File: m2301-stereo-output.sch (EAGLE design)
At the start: 77 parts, among them U1 ERM1-5MM, U2 ERM1-5MM, U3 ERM1-5MM, U4 G3VM-62C1

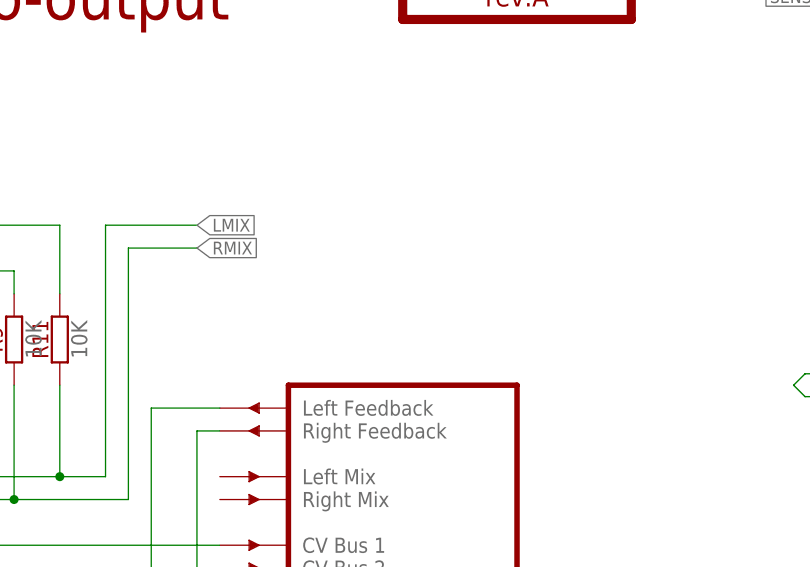
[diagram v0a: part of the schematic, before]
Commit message: Add (dummy) FX2 connectors to sch
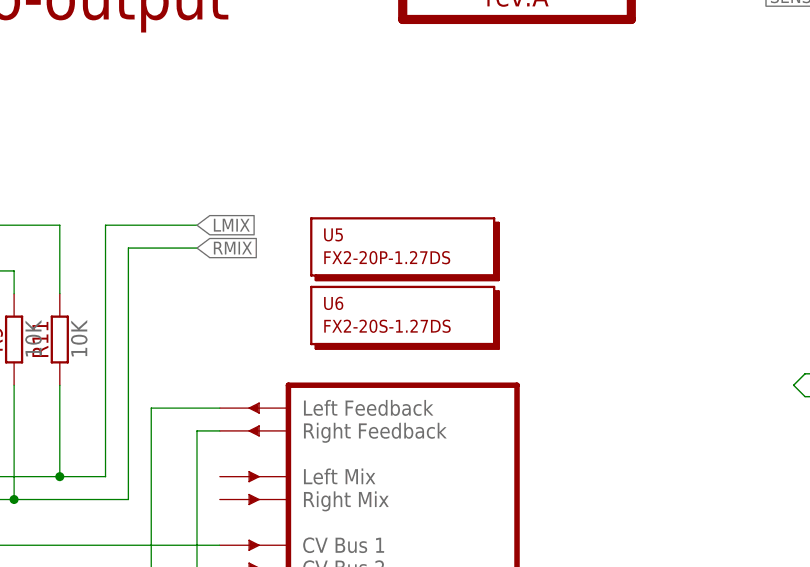
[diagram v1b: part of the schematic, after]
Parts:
- added U5: FX2-20P-1.27DS, hardware:FX2-20P-1.27DS
- added U6: FX2-20S-1.27DS, hardware:FX2-20S-1.27DS
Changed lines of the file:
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@@
 <part name="PWR6" library="supply" deviceset="-15V" device=""/>
 <part name="PWR7" library="supply" deviceset="-15V" device=""/>
+<part name="U5" library="hardware" deviceset="?" device="FX2-20P-1.27DS"/>
+<part name="U6" library="hardware" deviceset="?" device="FX2-20S-1.27DS"/>
 </parts>
 <sheets>
@@
 <instance part="PWR6" gate="G$1" x="160.02" y="-68.58" rot="R270"/>
 <instance part="PWR7" gate="G$1" x="160.02" y="-116.84" rot="R270"/>
+<instance part="U5" gate="G$1" x="109.22" y="12.7"/>
+<instance part="U6" gate="G$1" x="109.22" y="5.08"/>
 </instances>
 <busses>

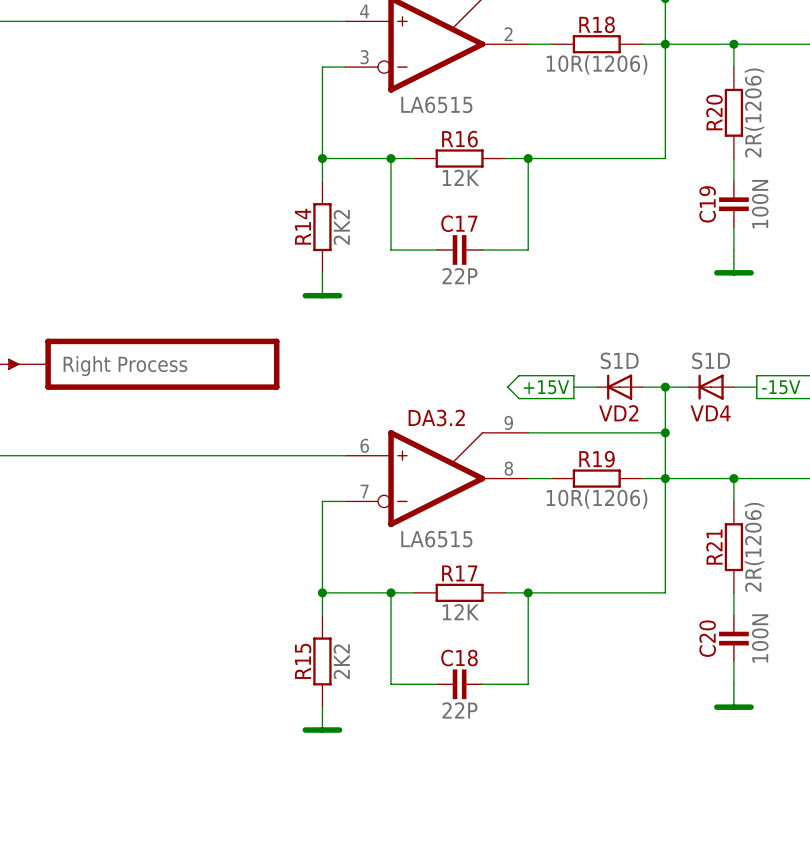
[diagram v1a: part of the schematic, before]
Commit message: Change headphone amplifier gain to +15 dB #4
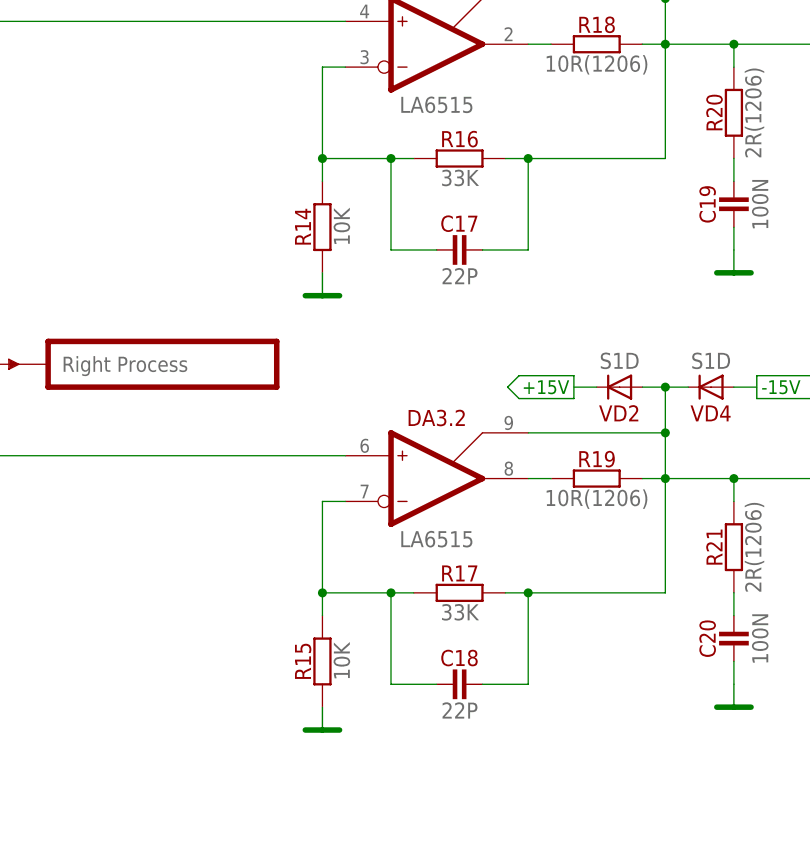
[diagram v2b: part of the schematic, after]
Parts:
- R14, R15: value 2K2 -> 10K; device resistors:2K2 -> resistors:10K
- R16, R17: value 12K -> 33K; device resistors:12K -> resistors:33K
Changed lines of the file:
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@@
 <?xml version="1.0" encoding="utf-8"?>
 <!DOCTYPE eagle SYSTEM "eagle.dtd">
-<eagle version="7.4.2">
+<eagle version="7.5.0">
 <drawing>
 <settings>
@@
 <part name="R19" library="resistors" deviceset="?" device="10R(1206)"/>
 <part name="DA3" library="ic-sanyo" deviceset="LA6515" device=""/>
-<part name="R14" library="resistors" deviceset="?" device="2K2"/>
-<part name="R15" library="resistors" deviceset="?" device="2K2"/>
-<part name="R16" library="resistors" deviceset="?" device="12K"/>
-<part name="R17" library="resistors" deviceset="?" device="12K"/>
+<part name="R14" library="resistors" deviceset="?" device="10K" value="10K"/>
+<part name="R15" library="resistors" deviceset="?" device="10K" value="10K"/>
+<part name="R16" library="resistors" deviceset="?" device="33K" value="33K"/>
+<part name="R17" library="resistors" deviceset="?" device="33K" value="33K"/>
 <part name="GND11" library="supply" deviceset="GND" device=""/>
 <part name="GND13" library="supply" deviceset="GND" device=""/>

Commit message: m2301 PCB update
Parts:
- removed HL1, HL2: WHITE(2MMX5MM), optoelectronics:WHITE(2MMX5MM)
- removed R24, R25: 100K, resistors:100K
- removed R27, R28: 680R, resistors:680R
- removed R3, R4: 10R(1206), resistors:10R(1206)
- removed U2, U3: ERM1-5MM, hardware:ERM1-5MM
- removed VD3, VD4: S1D, diodes:S1D
- removed VD6, VD7: MMSD4148, diodes:MMSD4148
- removed VT1, VT2: BC848, transistors-npn:BC848
- added C24, C25, C26, C27, C28: 100N, capacitors:100N
- added DA5: LM2903M, ic-fairchild:LM2903M
- added HL4: RED/BLUE(2MMX5MM,CC), optoelectronics:RED/BLUE(2MMX5MM,CC)
- added L1, L2: BLM31AJ601SN1L, inductors:BLM31AJ601SN1L
- added R30, R31: 10M, resistors:10M
- added R32, R33: 100K, resistors:100K
- added R34, R35: 47K, resistors:47K
- added R36: 330K, resistors:330K
- added R37: 22K, resistors:22K
- added R38: 4K7, resistors:4K7
- added R39: 100R, resistors:100R
- added R40: 2K2, resistors:2K2
- added R41: 10K, resistors:10K
- added R42: 1K8, resistors:1K8
- added U7: ERM1-5MM, hardware:ERM1-5MM
- added VD8, VD9: BAS16, diodes:BAS16
- added VT3: BC848, transistors-npn:BC848
- C11, C9: value 47U/35V -> 33U/25V; device capacitors-electrolytic:47U/35V -> capacitors-electrolytic:33U/25V
- PCB1: value rev.A -> rev.B
- VD1, VD2: value S1D -> BAV199; device diodes:S1D -> diodes:BAV199
- VD5: value MMSD4148 -> BAS16; device diodes:MMSD4148 -> diodes:BAS16
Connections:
- removed net N$30: R25.1, VD7.C, VT2.B
- removed net N$32: R28.1, VT2.C
- removed net N$33: HL2.C, R28.2
- removed net N$34: R24.1, VD6.C, VT1.B
- removed net N$35: R27.1, VT1.C
- removed net N$37: HL1.C, R27.2
- new net N$13: R34.2, VD8.A
- new net N$17: C24.2, R30.1, R32.2, R34.1
- new net N$18: C25.2, R31.1, R33.2, R35.1
- new net N$20: R35.2, VD9.A
- new net N$21: C26.2, DA5.1.IN+, DA5.2.IN+, R36.2, VD8.C, VD9.C
- new net N$23: DA5.1.IN-, R38.1, R39.2
- new net N$25: DA5.1.OUT, HL4.A2, R42.1, VT3.C
- new net N$47: DA5.2.IN-, R37.1, R38.2
- new net N$48: DA5.2.OUT, HL4.A1, R40.1, R41.2
- new net N$49: R41.1, VT3.B
- net +15V: now also C27.2, DA5*.V+, L1.2, R30.2, R31.2, R37.2; no longer HL1.A, HL2.A, R3.2
- net -15V: now also C28.1, DA5*.V-, HL4.K, L2.2, VD1.A, VD2.A, VT3.E; no longer R4.2, VD3.A, VD4.A
- net GND: now also C26.1, C27.1, C28.2, R32.1, R33.1, R36.1, R39.1, R40.2, R42.2; no longer VD6.A, VD7.A, VT1.E, VT2.E
- net N$1: now also L1.1; no longer R3.1
- net N$10: now also C25.1
- net N$11: now also VD1.CMN; no longer R24.2, VD1.A, VD3.C
- net N$15: now also C24.1
- net N$24: now also VD2.CMN; no longer R25.2, VD2.A, VD4.C
- net N$5: now also L2.1; no longer R4.1
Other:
- moved on the sheet: XS1
